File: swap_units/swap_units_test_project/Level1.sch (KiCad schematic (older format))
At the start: 3 parts, among them U1 LM324

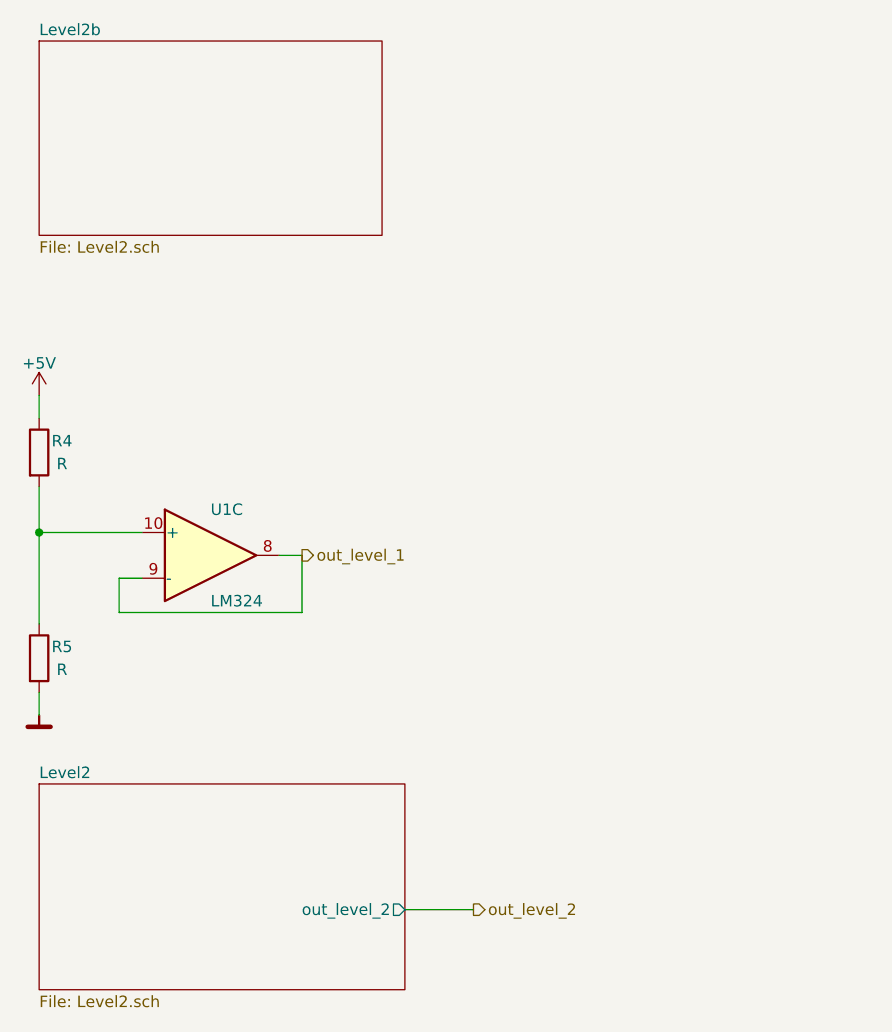
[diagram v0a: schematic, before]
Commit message: Moved and modified test project
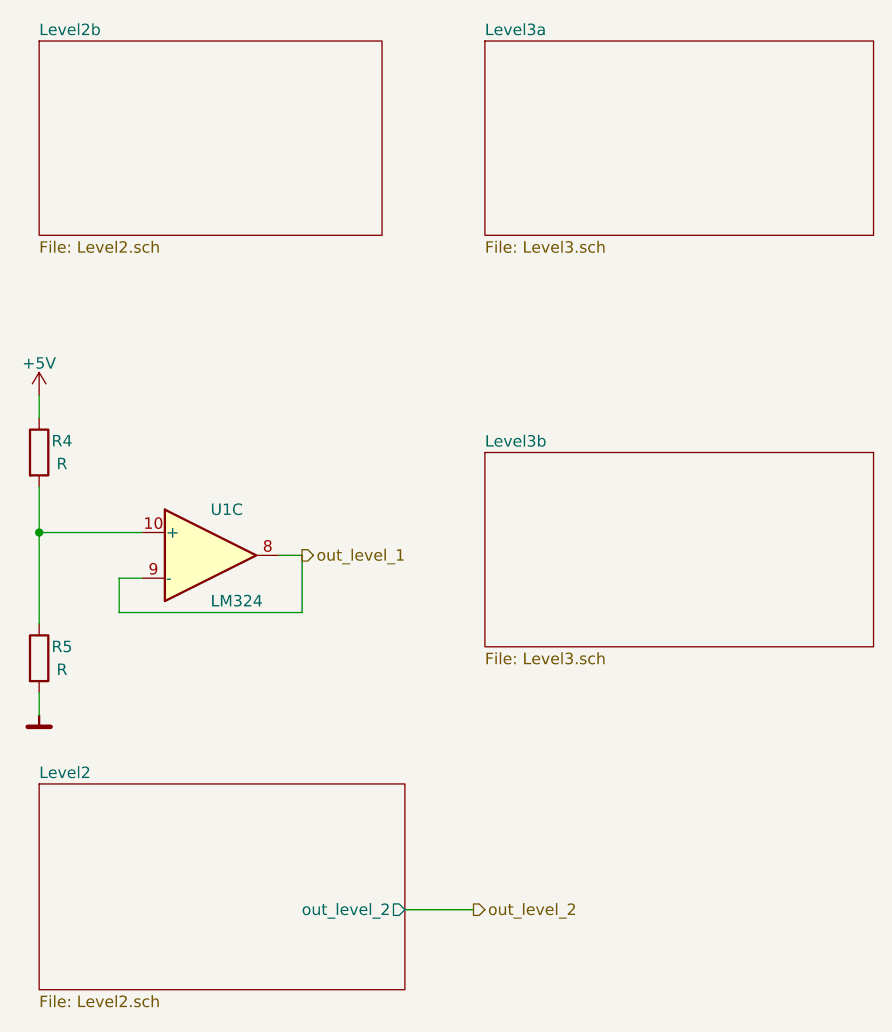
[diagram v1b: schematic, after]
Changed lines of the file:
@@
 $Descr A4 11693 8268
 encoding utf-8
-Sheet 2 4
+Sheet 2 6
 Title ""
 Date ""
@@
 F1 "Level2.sch" 50
 $EndSheet
+$Sheet
+S 4500 1300 1700 850
+U 5CB4DE53
+F0 "Level3a" 50
+F1 "Level3.sch" 50
+$EndSheet
+$Sheet
+S 4500 3100 1700 850
+U 5CB51184
+F0 "Level3b" 50
+F1 "Level3.sch" 50
+$EndSheet
 $EndSCHEMATC
